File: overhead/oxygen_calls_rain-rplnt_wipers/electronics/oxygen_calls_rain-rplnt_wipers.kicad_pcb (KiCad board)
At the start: 2 copper layers, 145 x 170.2 mm, 85 parts, among them J1 Conn_02x01, J2 Conn_02x11_Counter_Clockwise, J3 Conn_02x01, J4 Conn_02x01, J5 Conn_02x01, J6 Conn_02x01, J7 Conn_02x01, J8 Conn_02x01, J9 Conn_02x02_Counter_Clockwise

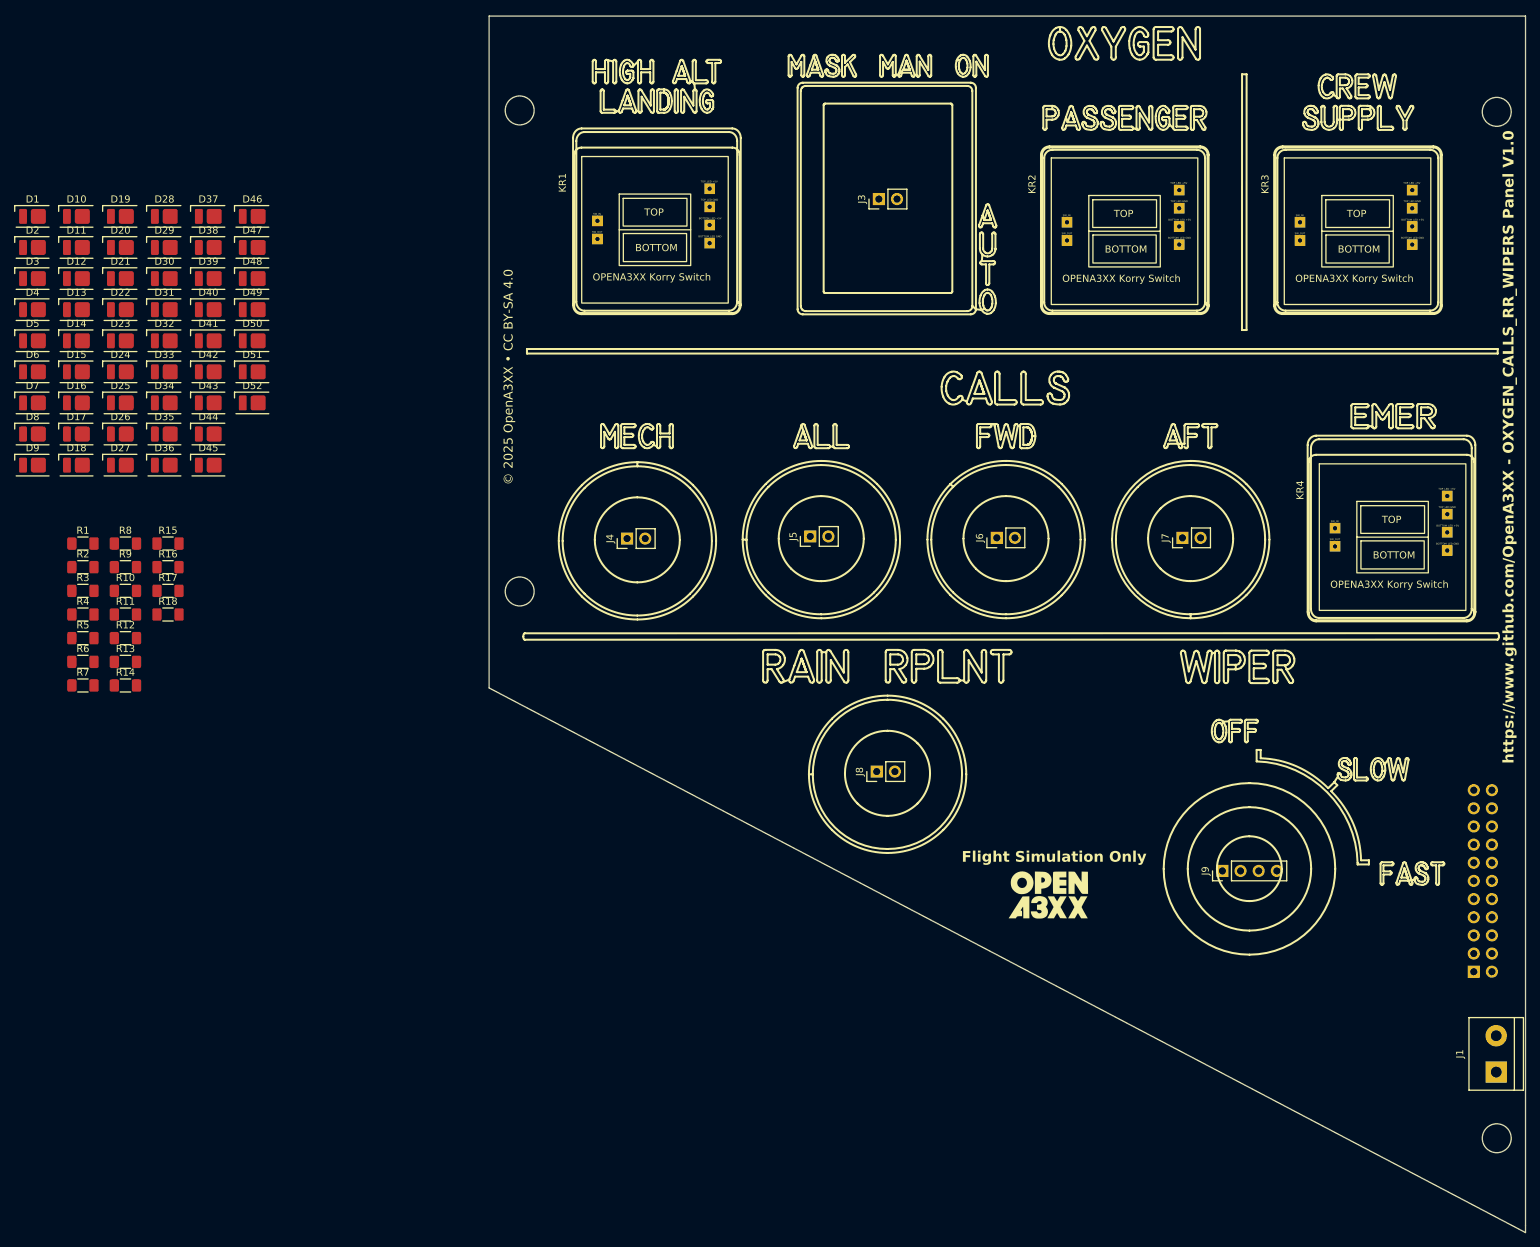
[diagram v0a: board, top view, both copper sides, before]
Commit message: Completed Oxygen_Calls_Rain Repellent & Wipers PCB + Changes to other designs
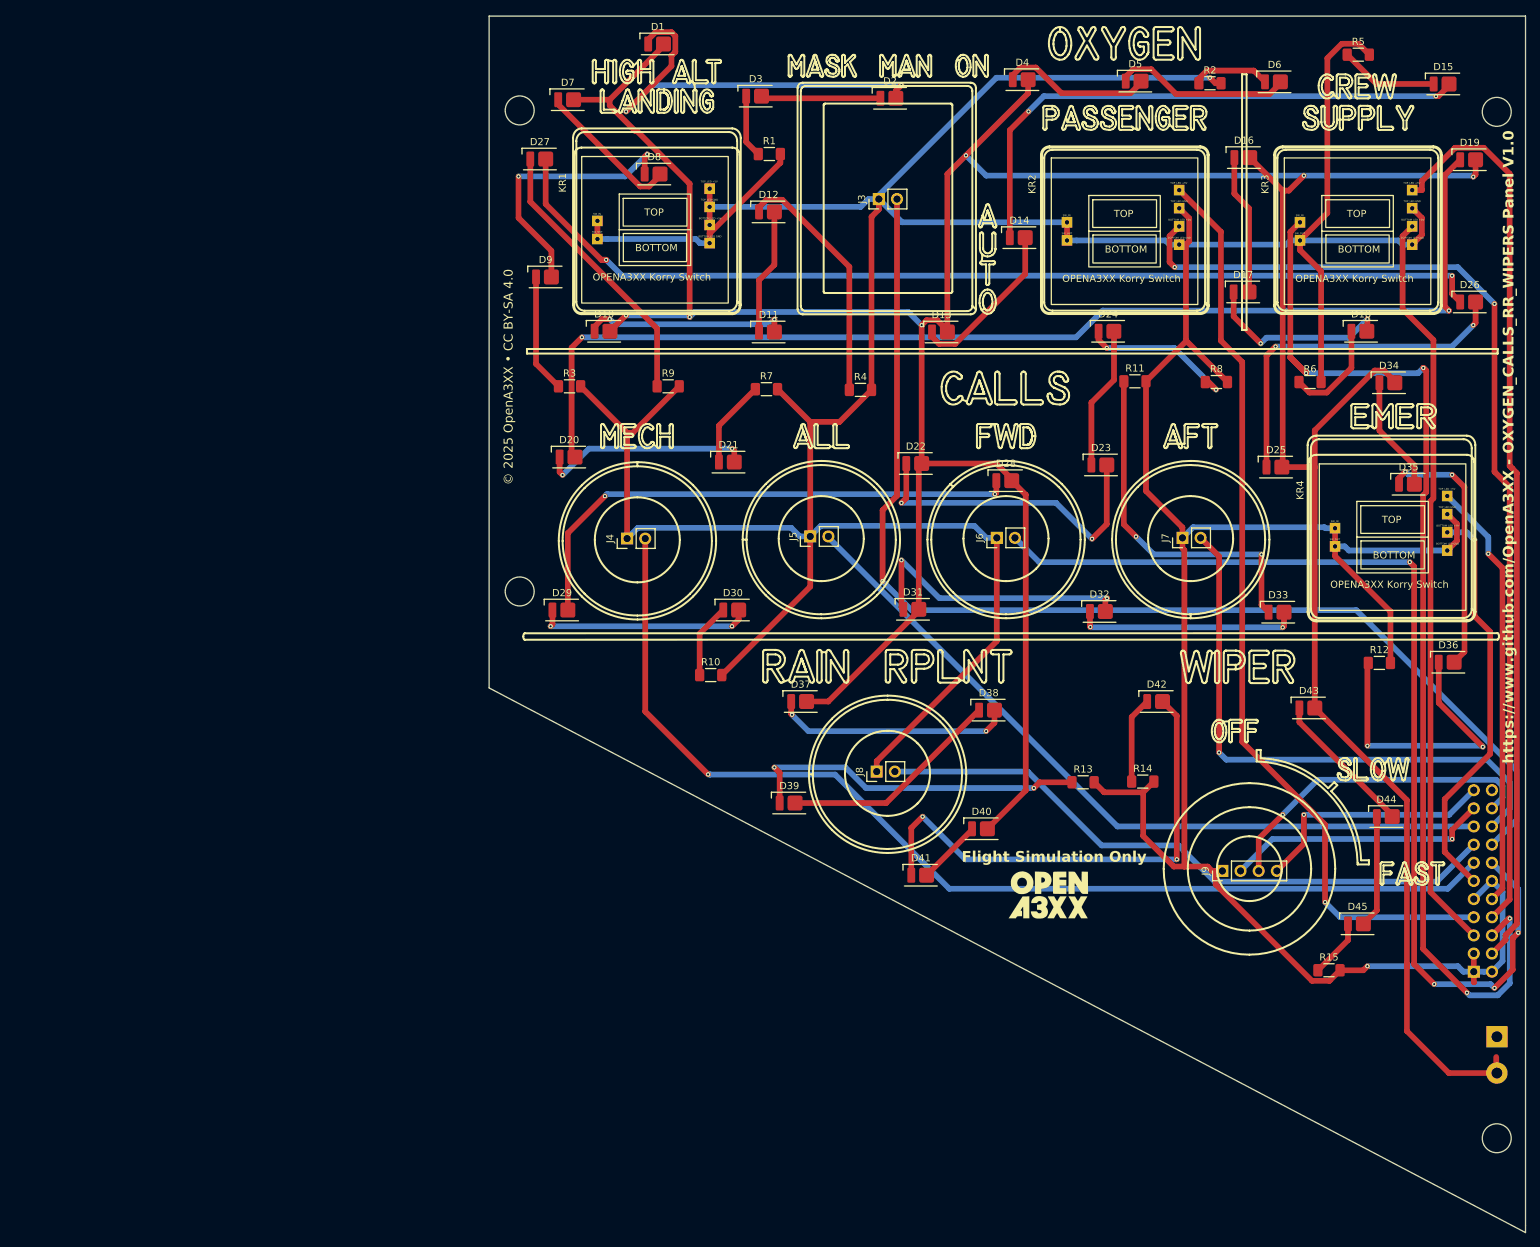
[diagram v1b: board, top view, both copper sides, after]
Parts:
- removed D46, D47, D48, D49, D50, D51, D52: LED, OpenA3XX:LED_Everlight-SMD3528_3.5x2.8mm_67-21ST
- removed R16, R17, R18: 220R, Resistor_SMD:R_1206_3216Metric_Pad1.30x1.75mm_HandSolder
- J1: moved to B.Cu
- moved R5 196.2 mm to (147.7, 27.6)
- moved D15 195.4 mm to (159.6, 31.7)
- moved D26 189.7 mm to (163.3, 62.2)
- moved D19 188.9 mm to (163.3, 42.3)
- moved D36 181.7 mm to (160.3, 112.6)
- moved D18 180.7 mm to (148.1, 66.3)
- moved D6 178.4 mm to (136.0, 31.4)
- moved R6 176.1 mm to (140.9, 73.4)
- moved R12 175.5 mm to (150.7, 112.7)
- moved D35 174.2 mm to (154.7, 87.7)
- moved D44 173.3 mm to (151.6, 134.2)
- moved D45 173.1 mm to (147.6, 149.2)
- moved R15 173.1 mm to (143.6, 155.7)
- moved R2 171.6 mm to (127.0, 31.6)
- moved D34 171.3 mm to (152.0, 73.5)
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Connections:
- D23 pad 2: +12V -> Net-(D22-K)
- D25 pad 2: Net-(D24-K) -> +12V
- D26 pad 2: +12V -> Net-(D25-K)
- D28 pad 2: Net-(D27-K) -> +12V
- D29 pad 2: +12V -> Net-(D28-K)
- D31 pad 2: Net-(D30-K) -> +12V
- D32 pad 2: +12V -> Net-(D31-K)
- D34 pad 2: Net-(D33-K) -> +12V
- D35 pad 2: +12V -> Net-(D34-K)
- D37 pad 2: Net-(D36-K) -> +12V
- D38 pad 2: +12V -> Net-(D37-K)
- D40 pad 2: Net-(D39-K) -> +12V
- D41 pad 2: +12V -> Net-(D40-K)
- D43 pad 2: Net-(D42-K) -> +12V
- D44 pad 2: +12V -> Net-(D43-K)
- R10 pad 1: Net-(D28-K) -> Net-(D30-K)
- R11 pad 1: Net-(D31-K) -> Net-(D33-K)
- R12 pad 1: Net-(D34-K) -> Net-(D36-K)
- R13 pad 1: Net-(D37-K) -> Net-(D39-K)
- R14 pad 1: Net-(D40-K) -> Net-(D42-K)
- R15 pad 1: Net-(D43-K) -> Net-(D45-K)
- R8 pad 1: Net-(D22-K) -> Net-(D24-K)
- R9 pad 1: Net-(D25-K) -> Net-(D27-K)
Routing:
- net GND: track 0.00 -> 744.9 mm, vias 0 -> 2
- net +12V: track 0.00 -> 518.9 mm, vias 0 -> 6
- net Net-(J2-Pin_16): track 0.00 -> 165.8 mm, vias 0 -> 1
- net Net-(J2-Pin_6): track 0.00 -> 163.8 mm, vias 0 -> 4
- net Net-(D19-K): track 0.00 -> 162.6 mm, vias 0 -> 2
- net Net-(J2-Pin_13): track 0.00 -> 151.9 mm, vias 0 -> 1
- net Net-(J2-Pin_14): track 0.00 -> 146.2 mm, vias 0 -> 4
- net Net-(D26-K): track 0.00 -> 144.1 mm, vias 0 -> 2
- net Net-(J2-Pin_8): track 0.00 -> 141.2 mm, vias 0 -> 2
- net Net-(J2-Pin_4): track 0.00 -> 129.9 mm
- net Net-(J2-Pin_7): track 0.00 -> 129.7 mm, vias 0 -> 1
- net Net-(J2-Pin_17): track 0.00 -> 107.2 mm
- net Net-(J2-Pin_5): track 0.00 -> 104.2 mm
- net Net-(J2-Pin_15): track 0.00 -> 89.5 mm
- net Net-(J2-Pin_18): track 0.00 -> 80.7 mm, vias 0 -> 1
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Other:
- board text added: "+12V Variable Backlight"
- board text added: "1-HIGH_ALT_LANDING-TOP_LED 2-HIGH_ALT_LANDING-BOTTOM_LED 3-HIGH_ALT_LANDING-KORRY_SW 4-PASSENGER-TOP_LED 5-PASSENGER-BOTTOM_LED 6-PASSENGER-KORRY_SW 7-CREW_SUPPLY-TOP_LED 8-CREW_SUPPLY-BOTTOM_LED 9-CREW_SUPPLY-KORRY_SW 10-CALL_EMER-TOP_LED 11-CALL_EMER-BOTTOM_LED"
- board text added: "12-CALL_EMER-KORRY_SW 13-MASK_MAN_ON_SW 14-CALLS_MECH_SW 15-CALLS_ALL_SW 16-CALLS_FWD_SW 17-CALLS_AFT_SW 18-RAIN_RPLNT_SW 19-WIPER_OFF_SW 20-WIPER_SLOW_SW 21-WIPER_FAST_SW"
- board text added: "GND"
